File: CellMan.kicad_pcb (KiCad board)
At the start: 2 copper layers, 99.1 x 45.7 mm, 54 parts, among them J1 Conn_01x05_Male, J2 IDC-Connector, J3 BalanceBusIn, J4 BalanceBusOut, M1 SMT-Standoff, M2 SMT-Standoff, M3 SMT-Standoff, M4 SMT-Standoff, Q1 SP8K24FRATB, T1 FlybackTransformer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

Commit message: Updated Schematic
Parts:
- removed R20: R, Resistor_SMD:R_0805_2012Metric_Pad1.15x1.40mm_HandSolder
- added C10: C, Capacitor_SMD:C_0805_2012Metric_Pad1.15x1.40mm_HandSolder, F.Cu at (84.0, 36.2)
- added C11: C, Capacitor_SMD:C_0805_2012Metric_Pad1.15x1.40mm_HandSolder, F.Cu at (88.9, 30.3)
- added JP1: Jumper, Connector_PinHeader_2.54mm:PinHeader_1x02_P2.54mm_Vertical_SMD_Pin1Left, F.Cu at (72.4, 49.3)
- added JP2: Jumper, Connector_PinHeader_2.54mm:PinHeader_1x02_P2.54mm_Vertical_SMD_Pin1Left, F.Cu at (80.4, 49.3)
- added JP3: SolderJumper_2_Open, Jumper:SolderJumper-2_P1.3mm_Open_RoundedPad1.0x1.5mm, F.Cu at (88.7, 33.6)
- added JP4: Jumper, Connector_PinHeader_2.54mm:PinHeader_1x02_P2.54mm_Vertical_SMD_Pin1Left, F.Cu at (72.4, 38.9)
- added Q2: SP8K24FRATB, Package_SO:SO-8_5.3x6.2mm_P1.27mm, F.Cu at (101.5, 32.7)
- added U4: MCP6001-OT, Package_TO_SOT_SMD:SOT-23-5, F.Cu at (79.3, 31.2)
- added U5: AD8479, Package_SO:SOIC-8_3.9x4.9mm_P1.27mm, F.Cu at (72.7, 32.1)
- C5: value 1uF 30V -> 1uF 50V; footprint Capacitor_SMD:C_0805_2012Metric_Pad1.15x1.40mm_HandSolder -> Capacitor_SMD:CP_Elec_4x5.4
- D3, D4: value PMEG3020DEP,115 -> 60V 2A; footprint Lafayette_Electric_Car_Footprints:Diode_PMEG3020DEP -> Lafayette_Electric_Car_Footprints:Diode_NTS260ESF
- F1, F2: footprint Lafayette_Electric_Car_Footprints:fuse_holder_smd_littelfuse -> Lafayette_Electric_Car_Footprints:0154.500DRL
- R18: value R -> 51k
- R19: value R -> 2.7k
- R21: value R -> 10k
- R4: value R -> 200
- R9: value R -> 5k
- U3: value MCP6004 -> ADM6320; footprint Package_SO:TSSOP-14_4.4x5mm_P0.65mm -> Package_TO_SOT_SMD:SOT-23-5_HandSoldering
- moved R17 88.5 mm to (84.1, 30.3), turned to 0 degrees
- moved R13 87.3 mm to (84.1, 33.3), turned to 0 degrees
- moved D4 82.5 mm to (116.2, 32.0), turned to 0 degrees
- moved C5 79.9 mm to (110.7, 31.8), turned to 0 degrees
- moved R14 79.4 mm to (79.3, 35.0), turned to 0 degrees
- moved D3 78.6 mm to (108.5, 37.9)
- moved R12 78.4 mm to (78.8, 37.9), turned to 0 degrees
- moved U3 74.8 mm to (71.4, 55.2)
- moved R11 74.1 mm to (76.6, 54.3), turned to 0 degrees
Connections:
- MCU1 pad 2: (no net) -> /DividedCell-
- MCU1 pad 6: (no net) -> /Watchdog
- R11 pad 1: Net-(R11-Pad1) -> +5V
- R11 pad 2: /CellVoltage -> Net-(R11-Pad2)
- R12 pad 1: GND -> +5V
- R13 pad 1: Net-(R13-Pad1) -> Net-(R12-Pad2)
- R13 pad 2: Net-(R11-Pad1) -> GND
- R14 pad 1: Net-(R14-Pad1) -> /Cell-
- R14 pad 2: Net-(R12-Pad2) -> Net-(R14-Pad2)
- R17 pad 1: /CellMeasurement/Divided_Cell- -> /Cell+
- R17 pad 2: GND -> Net-(JP3-Pad1)
- R18 pad 1: /CellMeasurement/Divided_Cell+ -> /DividedCell-
- R18 pad 2: GND -> /CellMeasurement/Seg-
- R19 pad 1: GND -> /CellMeasurement/Seg-
- R21 pad 1: /Cell+ -> Net-(R14-Pad2)
- R21 pad 2: /CellMeasurement/Divided_Cell+ -> /DividedCell-
- U3 pad 1: (no net) -> /Reset
- U3 pad 2: (no net) -> GND
- U3 pad 3: (no net) -> Net-(R11-Pad2)
- U3 pad 4: GND -> /Watchdog
- U3 pad 5: /CellMeasurement/Divided_Cell- -> +5V
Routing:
- net /DividedCell-: track 0.00 -> 45.5 mm
- net /CellMeasurement/Divided_Cell+: track 45.5 -> 0.00 mm
- net /CellMeasurement/Seg-: track 0.00 -> 8.89 mm, vias 0 -> 2
- net GND: track 75.1 -> 66.2 mm, vias 14 -> 12

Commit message: Start of new layout
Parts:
- moved R17 114.5 mm to (166.7, 109.6), turned to 90 degrees
- moved JP1 106.1 mm to (164.0, 102.9)
- moved JP3 93.4 mm to (114.4, 123.4)
- moved Q2 92.5 mm to (125.5, 122.1)
- moved JP4 89.8 mm to (114.7, 118.1)
- moved U5 88.1 mm to (131.5, 97.6), turned to 90 degrees
- moved C5 85.7 mm to (138.9, 112.7), turned to 270 degrees
- moved C11 84.8 mm to (135.9, 100.9), turned to 270 degrees
- moved R14 84.8 mm to (114.7, 112.0)
- moved U4 82.9 mm to (125.6, 100.0), turned to 90 degrees
- moved D4 78.4 mm to (138.5, 107.2), turned to 270 degrees
- moved R12 74.8 mm to (126.5, 95.6), turned to 270 degrees
- moved R13 74.2 mm to (124.5, 95.6), turned to 90 degrees
- moved D3 73.3 mm to (138.7, 104.7), turned to 90 degrees
- moved C10 70.7 mm to (122.4, 95.6), turned to 90 degrees
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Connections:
- D1 pad 1: GND -> /TSV_RTN
- R1 pad 1: GND -> /TSV_RTN
- R18 pad 2: /CellMeasurement/Seg- -> GND
- R19 pad 1: /CellMeasurement/Seg- -> GND
- R5 pad 2: GND -> /TSV_RTN
- R6 pad 2: GND -> /TSV_RTN
- R7 pad 2: GND -> /TSV_RTN
- R8 pad 1: GND -> /TSV_RTN
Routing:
- net +5V: track 110.1 -> 25.9 mm, vias 6 -> 1
- net /Cell+: track 66.7 -> 4.72 mm
- net /Cell-: track 48.8 -> 3.90 mm, vias 10 -> 2
- net /DividedCell-: track 45.5 -> 2.80 mm
- net Net-(D5-Pad2): track 37.6 -> 0.00 mm
- net /Balance_ctl: track 36.8 -> 1.10 mm, vias 2 -> 0
- net /CellTemp: track 33.4 -> 0.00 mm, vias 2 -> 0
- net Net-(Q1-Pad5): track 32.0 -> 0.00 mm, vias 5 -> 0
- net /SWIM: track 28.2 -> 0.00 mm
- net /Balance_current: track 26.1 -> 0.00 mm, vias 2 -> 0
- net /Reset: track 24.1 -> 0.00 mm
- net GND: track 66.2 -> 43.5 mm, vias 12 -> 3
- net Net-(ISO1-Pad3): track 24.5 -> 2.37 mm
- net /CellMeasurement/Vref: track 0.00 -> 19.4 mm
- net /CellVoltage: track 16.7 -> 0.07 mm
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- removed copper zone on B.Cu, net /Cell-(RAW)
- removed copper zone on F.Cu, net /Cell-(RAW)

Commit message: WIP 1/19
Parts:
- moved C9 2.59 mm to (129.1, 90.2)
- moved C6 2.54 mm to (131.1, 90.2)
- moved R15 1.96 mm to (127.1, 90.2)
- moved D1 1.93 mm to (125.0, 90.2)
- moved U5 1.22 mm to (130.6, 98.5)
- moved C10 0.90 mm to (121.7, 96.2)
- moved R12 0.90 mm to (125.8, 96.2)
- moved R13 0.90 mm to (123.8, 96.2)
- moved U4 0.90 mm to (124.9, 100.6)
- moved R19 0.65 mm to (122.9, 90.2)
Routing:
- net /Reset: track 0.00 -> 25.8 mm
- net /Watchdog: track 0.00 -> 24.9 mm
- net /CellTemp: track 0.00 -> 13.6 mm, vias 0 -> 2
- net /CellVoltage: track 0.07 -> 9.81 mm, vias 0 -> 2
- net +5V: track 25.9 -> 16.6 mm
- net /User_LED: track 10.3 -> 12.3 mm, vias 2 -> 0
- net /Cell-: track 3.90 -> 5.59 mm, vias 2 -> 3
- net /Ref_Cap: track 5.81 -> 7.30 mm
- net /Cell+: track 4.72 -> 3.24 mm
- net GND: track 43.5 -> 42.1 mm
- net /Balance_ctl: track 1.10 -> 0.00 mm

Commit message: 9 Unrouted Traces?
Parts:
- removed C10: C, Capacitor_SMD:C_0805_2012Metric_Pad1.15x1.40mm_HandSolder
- removed R13: R, Resistor_SMD:R_0805_2012Metric_Pad1.15x1.40mm_HandSolder
- removed U4: MCP6001-OT, Package_TO_SOT_SMD:SOT-23-5
- added VREF1: ADR510, Package_TO_SOT_SMD:SOT-23, F.Cu at (123.8, 100.0)
- D5: value D -> 60V 2A; footprint Lafayette_Electric_Car_Footprints:Diode_PMEG3020DEP -> Lafayette_Electric_Car_Footprints:Diode_NTS260ESF
- moved JP3 54.0 mm to (164.7, 103.9), turned to 180 degrees
- moved JP4 46.4 mm to (159.4, 105.7), turned to 180 degrees
- moved C11 12.3 mm to (124.6, 96.1)
- moved R14 10.5 mm to (123.8, 106.6), turned to 90 degrees
- moved JP1 10.3 mm to (169.2, 94.0), turned to 90 degrees
- moved D2 8.27 mm to (161.5, 118.2), turned to 0 degrees
- moved J3 6.36 mm to (146.5, 102.0)
- moved R16 5.57 mm to (161.5, 116.1), turned to 180 degrees
- moved F1 4.98 mm to (177.6, 114.3), turned to 0 degrees
- moved C3 4.17 mm to (130.0, 123.6)
- moved C4 4.17 mm to (132.2, 123.6)
- moved R2 4.07 mm to (133.8, 100.3)
- moved R3 4.07 mm to (135.8, 100.3)
- moved D4 3.77 mm to (134.8, 107.5)
- moved R10 3.77 mm to (161.5, 122.3)
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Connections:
- net Net-(D5-Pad2) renamed /CellBalancing/ThisOneToo
- net Net-(Q1-Pad5) renamed /CellBalancing/ThisNetNeedsAName
- D1 pad 1: /TSV_RTN -> GND
- R12 pad 2: Net-(R12-Pad2) -> /CellMeasurement/Vref
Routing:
- net +5V: track 16.6 -> 101.7 mm, vias 1 -> 8
- net /Cell+: track 3.24 -> 80.6 mm, vias 0 -> 2
- net GND: track 42.1 -> 108.2 mm, vias 3 -> 14
- net Net-(ISO1-Pad3): track 2.37 -> 48.1 mm, vias 0 -> 2
- net /Balance_ctl: track 0.00 -> 39.6 mm, vias 0 -> 2
- net /DividedCell-: track 2.80 -> 28.7 mm
- net /CellTemp: track 13.6 -> 39.4 mm
- net /SWIM: track 0.00 -> 25.6 mm, vias 0 -> 1
- net Net-(JP3-Pad2): track 0.00 -> 23.5 mm, vias 0 -> 1
- net /Balance_current: track 0.00 -> 21.5 mm, vias 0 -> 1
- net /Cell-: track 5.59 -> 20.7 mm, vias 3 -> 8
- net /Cell-(RAW): track 0.00 -> 14.4 mm
- net /Seg+: track 23.5 -> 36.0 mm
- net /CellVoltage: track 9.81 -> 21.6 mm, vias 2 -> 1
- net /Cell+(RAW): track 1.17 -> 12.9 mm
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- added copper zone on F.Cu, net /CellBalancing/ThisNetNeedsAName
- added copper zone on F.Cu, net /CellBalancing/ThisOneToo

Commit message: Who Cares
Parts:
- removed ISO1: VOM617A, Package_SO:SOP-4_3.8x4.1mm_P2.54mm
- removed J4: BalanceBusOut, Connector_PinHeader_2.54mm:PinHeader_1x02_P2.54mm_Vertical
- removed Q2: SP8K24FRATB, Package_SO:SO-8_5.3x6.2mm_P1.27mm
- removed R4: 200, Resistor_SMD:R_0805_2012Metric_Pad1.15x1.40mm_HandSolder
- removed R9: 5k, Resistor_SMD:R_0805_2012Metric_Pad1.15x1.40mm_HandSolder
- removed U3: ADM6320, Package_TO_SOT_SMD:SOT-23-5_HandSoldering
- added C10: 0.1uF 250V, Capacitor_SMD:C_1206_3216Metric_Pad1.42x1.75mm_HandSolder, F.Cu at (159.5, 122.6)
- added D6: 60V 2A, Lafayette_Electric_Car_Footprints:Diode_NTS260ESF, F.Cu at (147.2, 121.7)
- added R13: R, Resistor_SMD:R_0805_2012Metric_Pad1.15x1.40mm_HandSolder, F.Cu at (147.2, 124.2)
- added R23: R, Resistor_SMD:R_0805_2012Metric_Pad1.15x1.40mm_HandSolder, F.Cu at (126.0, 97.5)
- added R24: R, Resistor_SMD:R_0805_2012Metric_Pad1.15x1.40mm_HandSolder, F.Cu at (126.0, 99.5)
- F1, F2: footprint Lafayette_Electric_Car_Footprints:0154.500DRL -> Lafayette_Electric_Car_Footprints:fuse_holder_smd_littelfuse
- J3: value BalanceBusIn -> AVX-IDC; footprint Connector_PinHeader_2.54mm:PinHeader_1x02_P2.54mm_Vertical -> Lafayette_Electric_Car_Footprints:AVX
- R19: value 2.7k -> 820
- moved M1 124.4 mm to (196.4, 162.7)
- moved M2 94.9 mm to (183.3, 162.5)
- moved TH1 74.7 mm to (183.9, 88.7)
- moved M4 64.9 mm to (191.6, 151.3)
- moved R19 61.1 mm to (183.8, 84.2), turned to 0 degrees
- moved M3 30.3 mm to (181.1, 152.0)
- moved R11 27.9 mm to (129.5, 113.3)
- moved JP2 17.0 mm to (121.8, 113.9)
- moved VREF1 14.2 mm to (113.0, 90.9), turned to 270 degrees
- moved R2 8.68 mm to (130.4, 108.3), turned to 180 degrees
- moved R12 8.29 mm to (116.2, 90.9)
- moved C11 8.27 mm to (116.5, 98.0), turned to 90 degrees
- moved D2 8.13 mm to (168.0, 123.0)
- moved R16 8.12 mm to (168.0, 121.0)
- moved R3 8.06 mm to (130.4, 106.3), turned to 0 degrees
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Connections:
- C1 pad 1: /TSV_9V -> +9V
- C11 pad 1: +5V -> +9V
- C5 pad 2: GND -> /Balance-
- J2 pad 1: /TSV_9V -> +9V
- J2 pad 6: /TSV_9V -> /Reset
- J3 pad 1: GND -> /Balance-
- JP2 pad 1: GND -> /Balance-
- MCU1 pad 6: /Watchdog -> (no net)
- R1 pad 1: /TSV_RTN -> GND
- R11 pad 1: +5V -> GND
- R11 pad 2: Net-(R11-Pad2) -> /Balance-
- R5 pad 2: /TSV_RTN -> GND
- R6 pad 2: /TSV_RTN -> GND
- R7 pad 2: /TSV_RTN -> GND
- R8 pad 1: /TSV_RTN -> GND
- T1 pad 5: GND -> /Balance-
- U1 pad 8: /TSV_9V -> +9V
- U5 pad 6: /CellVoltage -> /CellMeasurement/CellVoltage_RAW
- U5 pad 7: +5V -> +9V
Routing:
- net /Cell+: track 80.6 -> 23.3 mm, vias 2 -> 8
- net +9V: track 0.00 -> 54.7 mm, vias 0 -> 3
- net GND: track 108.2 -> 62.0 mm, vias 14 -> 10
- net /Balance-: track 0.00 -> 35.1 mm
- net /TSV_9V: track 32.2 -> 0.00 mm
- net /Balance_ctl: track 39.6 -> 11.7 mm
- net Net-(JP3-Pad2): track 23.5 -> 48.4 mm, vias 1 -> 2
- net +5V: track 101.7 -> 77.2 mm, vias 8 -> 3
- net /Watchdog: track 23.7 -> 0.00 mm
- net /Balance_feedback: track 2.01 -> 20.2 mm, vias 0 -> 2
- net /A0: track 1.51 -> 17.0 mm, vias 1 -> 2
- net /SWIM: track 25.6 -> 38.5 mm, vias 1 -> 0
- net /CellMeasurement/Vref: track 14.3 -> 26.5 mm
- net /Balance_current: track 21.5 -> 33.1 mm, vias 1 -> 2
- net /TSV_RTN: track 8.55 -> 0.00 mm
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- added copper zone on B.Cu, net /Cell+
- added copper zone on F.Cu, net /Cell+
- added copper zone on F.Cu, net /Cell-
- removed copper zone on B.Cu, net /Cell+(RAW)
- removed copper zone on F.Cu, net /Cell+(RAW)
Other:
- board text added: "CellMan v2.2"
- board text removed: "CellMan v1.4"

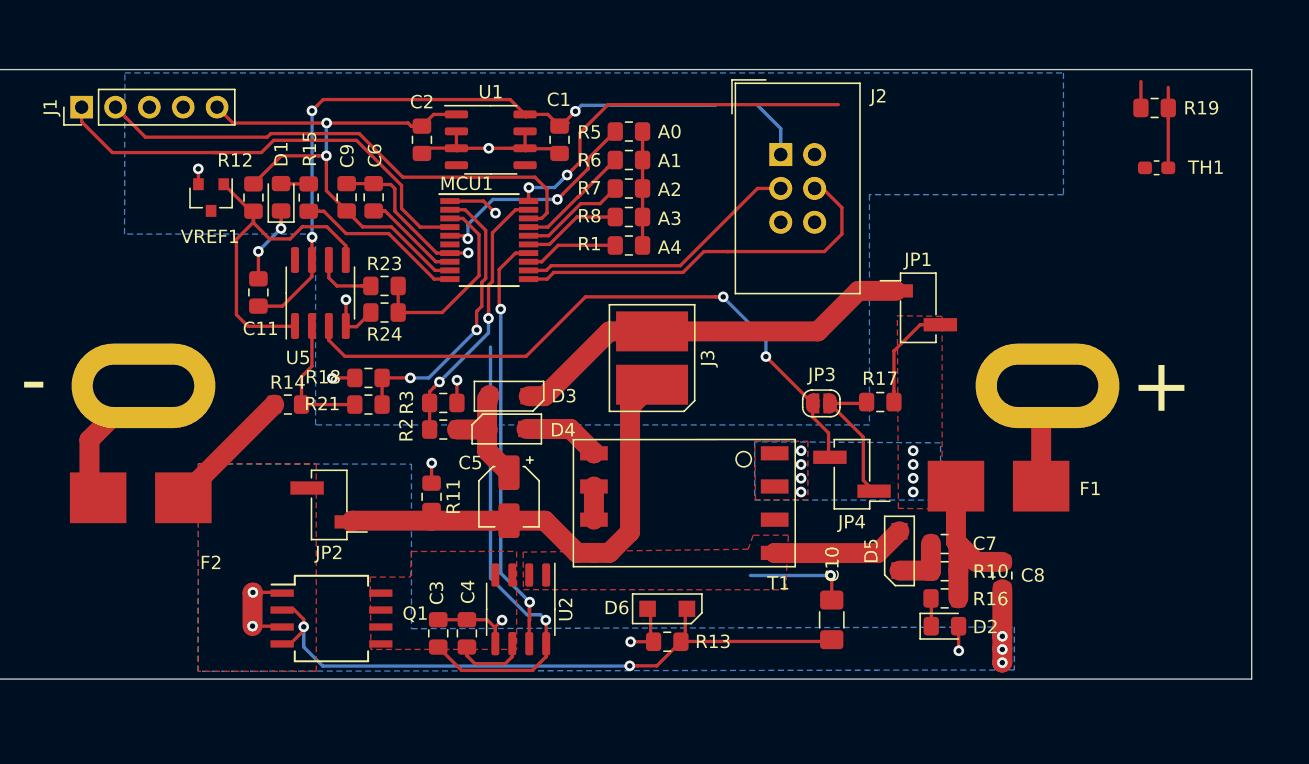
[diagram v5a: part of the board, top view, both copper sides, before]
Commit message: Traces Routed
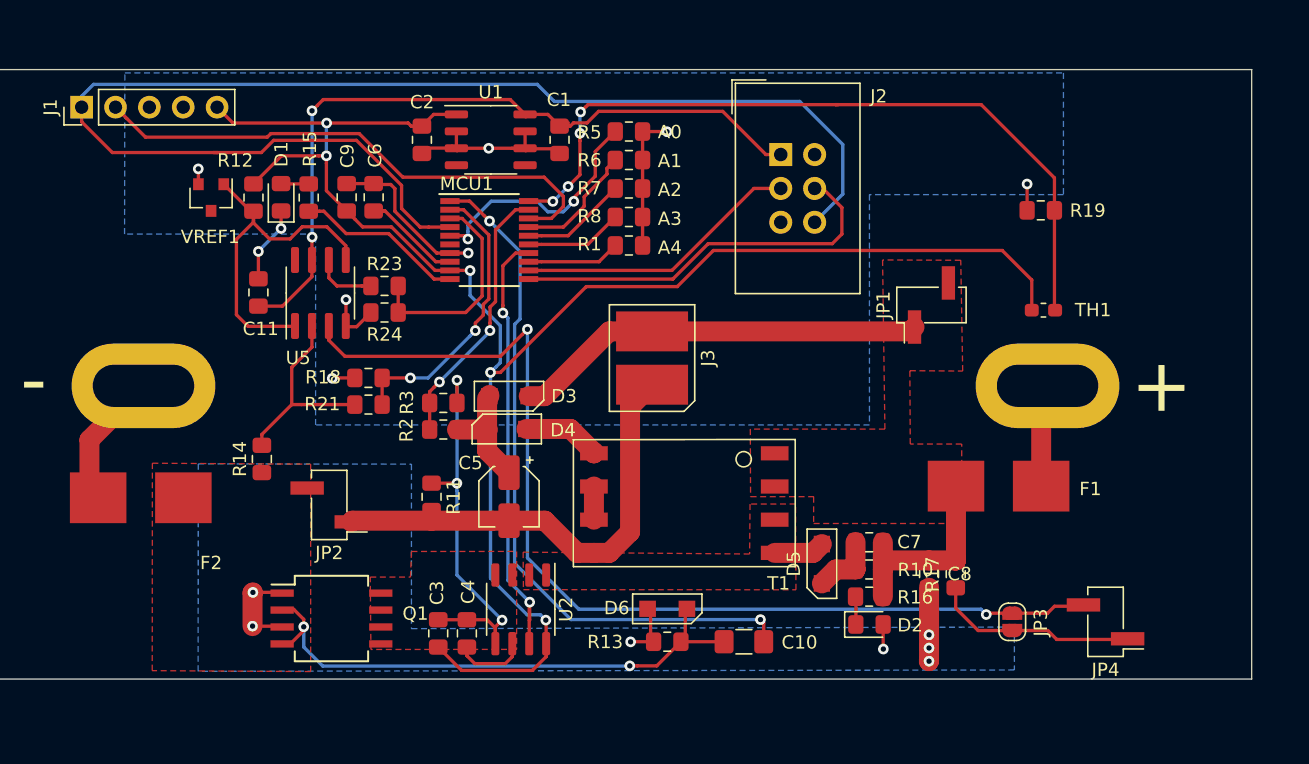
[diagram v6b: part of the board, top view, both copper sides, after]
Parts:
- moved JP4 22.0 mm to (180.1, 122.7)
- moved JP3 21.8 mm to (173.1, 122.7), turned to 90 degrees
- moved R17 14.1 mm to (168.8, 119.1), turned to 270 degrees
- moved TH1 13.6 mm to (175.4, 99.3)
- moved R19 11.5 mm to (175.2, 91.8)
- moved C10 6.79 mm to (152.9, 124.2), turned to 0 degrees
- moved D5 5.90 mm to (158.8, 118.3)
- moved C7 5.66 mm to (162.3, 116.7)
- moved D2 5.66 mm to (162.4, 122.9)
- moved R10 5.66 mm to (162.3, 118.8)
- moved R16 5.66 mm to (162.3, 120.8)
- moved C8 5.50 mm to (166.8, 119.1)
- moved R14 4.52 mm to (116.8, 110.5), turned to 90 degrees
- moved JP1 1.01 mm to (167.0, 98.9), turned to 90 degrees
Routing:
- net /Reset: track 34.0 -> 100.9 mm
- net +5V: track 77.2 -> 133.3 mm, vias 3 -> 5
- net /Balance_ctl: track 11.7 -> 52.3 mm
- net Net-(JP3-Pad2): track 48.4 -> 78.2 mm
- net /CellTemp: track 34.1 -> 57.6 mm, vias 2 -> 4
- net GND: track 62.0 -> 83.6 mm, vias 10 -> 12
- net /Cell-: track 28.1 -> 18.5 mm
- net Net-(C10-Pad1): track 50.6 -> 42.5 mm
- net /CellBalancing/ThisOneToo: track 10.0 -> 3.81 mm
- net /Cell+: track 23.3 -> 18.0 mm, vias 8 -> 0
- net Net-(R14-Pad2): track 10.2 -> 15.2 mm
- net Net-(JP3-Pad1): track 10.8 -> 15.4 mm
- net /SWIM: track 38.5 -> 40.4 mm
- net +9V: track 54.7 -> 56.4 mm, vias 3 -> 2
- net /A0: track 17.0 -> 18.4 mm
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- removed copper zone on B.Cu, net /Cell+

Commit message: Added Flair
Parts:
- added LOGO1: LafECEDepLogo, Lafayette_Electric_Car_Footprints:ECE_Logo_Jon, B.Cu at (137.4, 87.5)
- added LOGO2: LeopardPawLogo, Lafayette_Electric_Car_Footprints:Paw, F.Cu at (101.3, 121.7)
- moved R19 4.20 mm to (175.2, 96.0)
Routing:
- net GND: track 83.6 -> 94.9 mm
- net /CellTemp: track 57.6 -> 54.1 mm
- net Net-(JP3-Pad2): track 78.2 -> 75.8 mm
- net /A0: track 18.4 -> 17.3 mm
- net /CellVoltage: track 16.2 -> 17.0 mm
- net /DividedCell-: track 21.8 -> 22.4 mm
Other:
- board text added: "Address Select"
- board text removed: "I2C Address"
